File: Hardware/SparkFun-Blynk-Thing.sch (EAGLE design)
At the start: 103 parts, among them IC1 LMV358, Q1 2.5A/30V, Q2 MMBT2222A, Q3 MMBT2222A, U1 MCP73831, U2 ESP8266, U3 AP2112K-3.3V, U4 FT231XS-U, U5 W25Q32FVSS, U6 SI7021, Y1 26MHz

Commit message: Adding PROD_ID's to U5 and JP14
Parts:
- JP14: PROD_ID TBD -> CONN-13230
- U5: PROD_ID (none) -> IC-13229
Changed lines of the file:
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@@
 <grid distance="0.1" unitdist="inch" unit="inch" style="lines" multiple="1" display="no" altdistance="0.01" altunitdist="inch" altunit="inch"/>
 <layers>
-<layer number="1" name="Top" color="4" fill="1" visible="yes" active="no"/>
-<layer number="2" name="Route2" color="1" fill="3" visible="yes" active="no"/>
-<layer number="3" name="Route3" color="4" fill="3" visible="yes" active="no"/>
-<layer number="4" name="Route4" color="1" fill="4" visible="yes" active="no"/>
-<layer number="5" name="Route5" color="4" fill="4" visible="yes" active="no"/>
-<layer number="6" name="Route6" color="1" fill="8" visible="yes" active="no"/>
-<layer number="7" name="Route7" color="4" fill="8" visible="yes" active="no"/>
-<layer number="8" name="Route8" color="1" fill="2" visible="yes" active="no"/>
-<layer number="9" name="Route9" color="4" fill="2" visible="yes" active="no"/>
-<layer number="10" name="Route10" color="1" fill="7" visible="yes" active="no"/>
-<layer number="11" name="Route11" color="4" fill="7" visible="yes" active="no"/>
-<layer number="12" name="Route12" color="1" fill="5" visible="yes" active="no"/>
-<layer number="13" name="Route13" color="4" fill="5" visible="yes" active="no"/>
-<layer number="14" name="Route14" color="1" fill="6" visible="yes" active="no"/>
-<layer number="15" name="Route15" color="4" fill="6" visible="yes" active="no"/>
-<layer number="16" name="Bottom" color="1" fill="1" visible="yes" active="no"/>
-<layer number="17" name="Pads" color="2" fill="1" visible="yes" active="no"/>
-<layer number="18" name="Vias" color="2" fill="1" visible="yes" active="no"/>
-<layer number="19" name="Unrouted" color="6" fill="1" visible="yes" active="no"/>
-<layer number="20" name="Dimension" color="15" fill="1" visible="yes" active="no"/>
-<layer number="21" name="tPlace" color="16" fill="1" visible="yes" active="no"/>
-<layer number="22" name="bPlace" color="14" fill="1" visible="yes" active="no"/>
-<layer number="23" name="tOrigins" color="15" fill="1" visible="yes" active="no"/>
-<layer number="24" name="bOrigins" color="15" fill="1" visible="yes" active="no"/>
-<layer number="25" name="tNames" color="7" fill="1" visible="yes" active="no"/>
-<layer number="26" name="bNames" color="7" fill="1" visible="yes" active="no"/>
-<layer number="27" name="tValues" color="7" fill="1" visible="yes" active="no"/>
-<layer number="28" name="bValues" color="7" fill="1" visible="yes" active="no"/>
+<layer number="1" name="Top" color="4" fill="1" visible="no" active="no"/>
+<layer number="2" name="Route2" color="1" fill="3" visible="no" active="no"/>
+<layer number="3" name="Route3" color="4" fill="3" visible="no" active="no"/>
+<layer number="4" name="Route4" color="1" fill="4" visible="no" active="no"/>
+<layer number="5" name="Route5" color="4" fill="4" visible="no" active="no"/>
+<layer number="6" name="Route6" color="1" fill="8" visible="no" active="no"/>
+<layer number="7" name="Route7" color="4" fill="8" visible="no" active="no"/>
+<layer number="8" name="Route8" color="1" fill="2" visible="no" active="no"/>
+<layer number="9" name="Route9" color="4" fill="2" visible="no" active="no"/>
+<layer number="10" name="Route10" color="1" fill="7" visible="no" active="no"/>
+<layer number="11" name="Route11" color="4" fill="7" visible="no" active="no"/>
+<layer number="12" name="Route12" color="1" fill="5" visible="no" active="no"/>
+<layer number="13" name="Route13" color="4" fill="5" visible="no" active="no"/>
+<layer number="14" name="Route14" color="1" fill="6" visible="no" active="no"/>
+<layer number="15" name="Route15" color="4" fill="6" visible="no" active="no"/>
+<layer number="16" name="Bottom" color="1" fill="1" visible="no" active="no"/>
+<layer number="17" name="Pads" color="2" fill="1" visible="no" active="no"/>
+<layer number="18" name="Vias" color="2" fill="1" visible="no" active="no"/>
+<layer number="19" name="Unrouted" color="6" fill="1" visible="no" active="no"/>
+<layer number="20" name="Dimension" color="15" fill="1" visible="no" active="no"/>
+<layer number="21" name="tPlace" color="16" fill="1" visible="no" active="no"/>
+<layer number="22" name="bPlace" color="14" fill="1" visible="no" active="no"/>
+<layer number="23" name="tOrigins" color="15" fill="1" visible="no" active="no"/>
+<layer number="24" name="bOrigins" color="15" fill="1" visible="no" active="no"/>
+<layer number="25" name="tNames" color="7" fill="1" visible="no" active="no"/>
+<layer number="26" name="bNames" color="7" fill="1" visible="no" active="no"/>
+<layer number="27" name="tValues" color="7" fill="1" visible="no" active="no"/>
+<layer number="28" name="bValues" color="7" fill="1" visible="no" active="no"/>
 <layer number="29" name="tStop" color="7" fill="3" visible="no" active="no"/>
 <layer number="30" name="bStop" color="7" fill="6" visible="no" active="no"/>
@@
 <layer number="35" name="tGlue" color="7" fill="4" visible="no" active="no"/>
 <layer number="36" name="bGlue" color="7" fill="5" visible="no" active="no"/>
-<layer number="37" name="tTest" color="7" fill="1" visible="yes" active="no"/>
-<layer number="38" name="bTest" color="7" fill="1" visible="yes" active="no"/>
+<layer number="37" name="tTest" color="7" fill="1" visible="no" active="no"/>
+<layer number="38" name="bTest" color="7" fill="1" visible="no" active="no"/>
 <layer number="39" name="tKeepout" color="4" fill="11" visible="no" active="no"/>
 <layer number="40" name="bKeepout" color="1" fill="11" visible="no" active="no"/>
@@
 <layer number="44" name="Drills" color="7" fill="1" visible="no" active="no"/>
 <layer number="45" name="Holes" color="7" fill="1" visible="no" active="no"/>
-<layer number="46" name="Milling" color="3" fill="1" visible="yes" active="no"/>
-<layer number="47" name="Measures" color="7" fill="1" visible="yes" active="no"/>
-<layer number="48" name="Document" color="7" fill="1" visible="yes" active="no"/>
-<layer number="49" name="Reference" color="7" fill="1" visible="yes" active="no"/>
-<layer number="50" name="dxf" color="7" fill="1" visible="yes" active="no"/>
-<layer number="51" name="tDocu" color="6" fill="1" visible="yes" active="no"/>
-<layer number="52" name="bDocu" color="7" fill="1" visible="yes" active="no"/>
-<layer number="53" name="tGND_GNDA" color="7" fill="9" visible="yes" active="no"/>
-<layer number="54" name="bGND_GNDA" color="1" fill="9" visible="yes" active="no"/>
-<layer number="56" name="wert" color="7" fill="1" visible="yes" active="no"/>
-<layer number="57" name="tCAD" color="7" fill="1" visible="yes" active="no"/>
-<layer number="59" name="tCarbon" color="7" fill="1" visible="yes" active="no"/>
-<layer number="60" name="bCarbon" color="7" fill="1" visible="yes" active="no"/>
+<layer number="46" name="Milling" color="3" fill="1" visible="no" active="no"/>
+<layer number="47" name="Measures" color="7" fill="1" visible="no" active="no"/>
+<layer number="48" name="Document" color="7" fill="1" visible="no" active="no"/>
+<layer number="49" name="Reference" color="7" fill="1" visible="no" active="no"/>
+<layer number="50" name="dxf" color="7" fill="1" visible="no" active="no"/>
+<layer number="51" name="tDocu" color="6" fill="1" visible="no" active="no"/>
+<layer number="52" name="bDocu" color="7" fill="1" visible="no" active="no"/>
+<layer number="53" name="tGND_GNDA" color="7" fill="9" visible="no" active="no"/>
+<layer number="54" name="bGND_GNDA" color="1" fill="9" visible="no" active="no"/>
+<layer number="56" name="wert" color="7" fill="1" visible="no" active="no"/>
+<layer number="57" name="tCAD" color="7" fill="1" visible="no" active="no"/>
+<layer number="59" name="tCarbon" color="7" fill="1" visible="no" active="no"/>
+<layer number="60" name="bCarbon" color="7" fill="1" visible="no" active="no"/>
 <layer number="90" name="Modules" color="5" fill="1" visible="yes" active="yes"/>
 <layer number="91" name="Nets" color="2" fill="1" visible="yes" active="yes"/>
@@
 <part name="SUPPLY15" library="SparkFun-Aesthetics" deviceset="VCC" device=""/>
 <part name="GND36" library="SparkFun-Aesthetics" deviceset="GND" device=""/>
-<part name="U5" library="blynk-thing-temp" deviceset="W25Q32FV" device="SS"/>
+<part name="U5" library="blynk-thing-temp" deviceset="W25Q32FV" device="SS">
+<attribute name="PROD_ID" value="IC-13229"/>
+</part>
 <part name="LOGO2" library="SparkFun-Aesthetics" deviceset="OSHW-LOGO" device="S" value="OSHW-LOGOS"/>
 <part name="E1" library="SparkFun-RF" deviceset="ANTENNA" device="TRACE" value="ANTENNATRACE"/>
@@
 <part name="D4" library="SparkFun-LED" deviceset="WS2812B" device="" value="WS2812"/>
 <part name="JP14" library="SparkFun-Connectors" deviceset="M03" device="JST-PTH-VERT">
-<attribute name="PROD_ID" value="TBD"/>
+<attribute name="PROD_ID" value="CONN-13230"/>
 </part>
 <part name="U6" library="SparkFun-Sensors" deviceset="SI7021" device=""/>

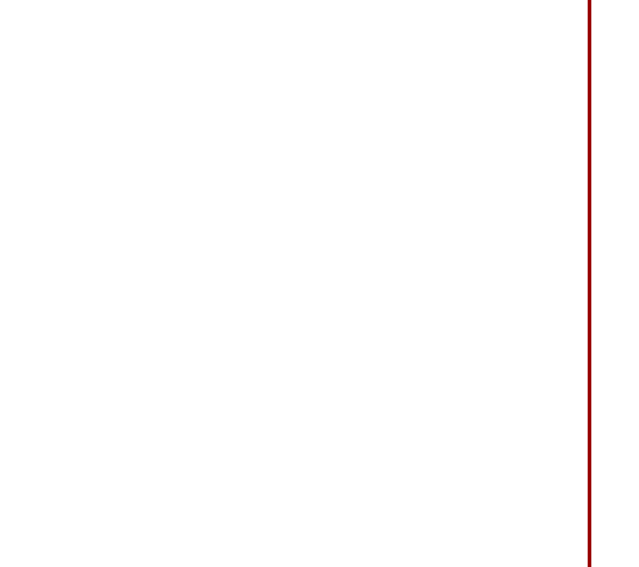
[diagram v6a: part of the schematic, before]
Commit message: Moving WS2812-VCC jumper.
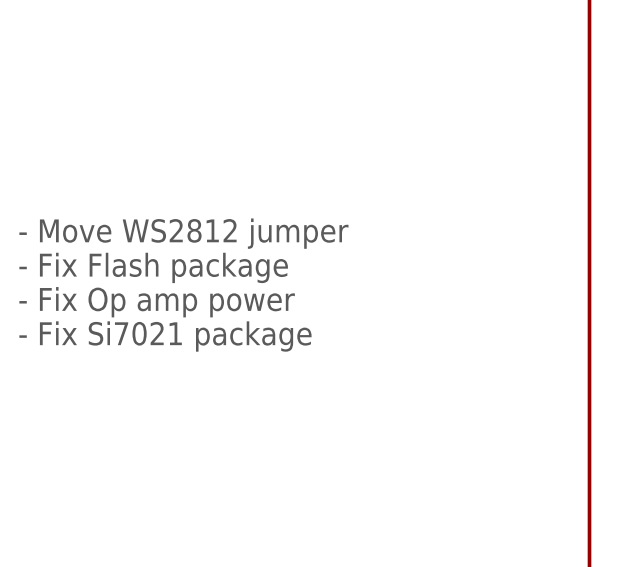
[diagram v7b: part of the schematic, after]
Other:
- note added: "- Move WS2812 jumper - Fix Flash package - Fix Op amp power - Fix Si7021 package"
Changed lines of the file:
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@@
 <grid distance="0.1" unitdist="inch" unit="inch" style="lines" multiple="1" display="no" altdistance="0.01" altunitdist="inch" altunit="inch"/>
 <layers>
-<layer number="1" name="Top" color="4" fill="1" visible="no" active="no"/>
-<layer number="2" name="Route2" color="1" fill="3" visible="no" active="no"/>
-<layer number="3" name="Route3" color="4" fill="3" visible="no" active="no"/>
-<layer number="4" name="Route4" color="1" fill="4" visible="no" active="no"/>
-<layer number="5" name="Route5" color="4" fill="4" visible="no" active="no"/>
-<layer number="6" name="Route6" color="1" fill="8" visible="no" active="no"/>
-<layer number="7" name="Route7" color="4" fill="8" visible="no" active="no"/>
-<layer number="8" name="Route8" color="1" fill="2" visible="no" active="no"/>
-<layer number="9" name="Route9" color="4" fill="2" visible="no" active="no"/>
-<layer number="10" name="Route10" color="1" fill="7" visible="no" active="no"/>
-<layer number="11" name="Route11" color="4" fill="7" visible="no" active="no"/>
-<layer number="12" name="Route12" color="1" fill="5" visible="no" active="no"/>
-<layer number="13" name="Route13" color="4" fill="5" visible="no" active="no"/>
-<layer number="14" name="Route14" color="1" fill="6" visible="no" active="no"/>
-<layer number="15" name="Route15" color="4" fill="6" visible="no" active="no"/>
-<layer number="16" name="Bottom" color="1" fill="1" visible="no" active="no"/>
-<layer number="17" name="Pads" color="2" fill="1" visible="no" active="no"/>
-<layer number="18" name="Vias" color="2" fill="1" visible="no" active="no"/>
-<layer number="19" name="Unrouted" color="6" fill="1" visible="no" active="no"/>
-<layer number="20" name="Dimension" color="15" fill="1" visible="no" active="no"/>
-<layer number="21" name="tPlace" color="16" fill="1" visible="no" active="no"/>
-<layer number="22" name="bPlace" color="14" fill="1" visible="no" active="no"/>
-<layer number="23" name="tOrigins" color="15" fill="1" visible="no" active="no"/>
-<layer number="24" name="bOrigins" color="15" fill="1" visible="no" active="no"/>
-<layer number="25" name="tNames" color="7" fill="1" visible="no" active="no"/>
-<layer number="26" name="bNames" color="7" fill="1" visible="no" active="no"/>
-<layer number="27" name="tValues" color="7" fill="1" visible="no" active="no"/>
-<layer number="28" name="bValues" color="7" fill="1" visible="no" active="no"/>
+<layer number="1" name="Top" color="4" fill="1" visible="yes" active="no"/>
+<layer number="2" name="Route2" color="1" fill="3" visible="yes" active="no"/>
+<layer number="3" name="Route3" color="4" fill="3" visible="yes" active="no"/>
+<layer number="4" name="Route4" color="1" fill="4" visible="yes" active="no"/>
+<layer number="5" name="Route5" color="4" fill="4" visible="yes" active="no"/>
+<layer number="6" name="Route6" color="1" fill="8" visible="yes" active="no"/>
+<layer number="7" name="Route7" color="4" fill="8" visible="yes" active="no"/>
+<layer number="8" name="Route8" color="1" fill="2" visible="yes" active="no"/>
+<layer number="9" name="Route9" color="4" fill="2" visible="yes" active="no"/>
+<layer number="10" name="Route10" color="1" fill="7" visible="yes" active="no"/>
+<layer number="11" name="Route11" color="4" fill="7" visible="yes" active="no"/>
+<layer number="12" name="Route12" color="1" fill="5" visible="yes" active="no"/>
+<layer number="13" name="Route13" color="4" fill="5" visible="yes" active="no"/>
+<layer number="14" name="Route14" color="1" fill="6" visible="yes" active="no"/>
+<layer number="15" name="Route15" color="4" fill="6" visible="yes" active="no"/>
+<layer number="16" name="Bottom" color="1" fill="1" visible="yes" active="no"/>
+<layer number="17" name="Pads" color="2" fill="1" visible="yes" active="no"/>
+<layer number="18" name="Vias" color="2" fill="1" visible="yes" active="no"/>
+<layer number="19" name="Unrouted" color="6" fill="1" visible="yes" active="no"/>
+<layer number="20" name="Dimension" color="15" fill="1" visible="yes" active="no"/>
+<layer number="21" name="tPlace" color="16" fill="1" visible="yes" active="no"/>
+<layer number="22" name="bPlace" color="14" fill="1" visible="yes" active="no"/>
+<layer number="23" name="tOrigins" color="15" fill="1" visible="yes" active="no"/>
+<layer number="24" name="bOrigins" color="15" fill="1" visible="yes" active="no"/>
+<layer number="25" name="tNames" color="7" fill="1" visible="yes" active="no"/>
+<layer number="26" name="bNames" color="7" fill="1" visible="yes" active="no"/>
+<layer number="27" name="tValues" color="7" fill="1" visible="yes" active="no"/>
+<layer number="28" name="bValues" color="7" fill="1" visible="yes" active="no"/>
 <layer number="29" name="tStop" color="7" fill="3" visible="no" active="no"/>
 <layer number="30" name="bStop" color="7" fill="6" visible="no" active="no"/>
@@
 <layer number="35" name="tGlue" color="7" fill="4" visible="no" active="no"/>
 <layer number="36" name="bGlue" color="7" fill="5" visible="no" active="no"/>
-<layer number="37" name="tTest" color="7" fill="1" visible="no" active="no"/>
-<layer number="38" name="bTest" color="7" fill="1" visible="no" active="no"/>
+<layer number="37" name="tTest" color="7" fill="1" visible="yes" active="no"/>
+<layer number="38" name="bTest" color="7" fill="1" visible="yes" active="no"/>
 <layer number="39" name="tKeepout" color="4" fill="11" visible="no" active="no"/>
 <layer number="40" name="bKeepout" color="1" fill="11" visible="no" active="no"/>
@@
 <layer number="44" name="Drills" color="7" fill="1" visible="no" active="no"/>
 <layer number="45" name="Holes" color="7" fill="1" visible="no" active="no"/>
-<layer number="46" name="Milling" color="3" fill="1" visible="no" active="no"/>
-<layer number="47" name="Measures" color="7" fill="1" visible="no" active="no"/>
-<layer number="48" name="Document" color="7" fill="1" visible="no" active="no"/>
-<layer number="49" name="Reference" color="7" fill="1" visible="no" active="no"/>
-<layer number="50" name="dxf" color="7" fill="1" visible="no" active="no"/>
-<layer number="51" name="tDocu" color="6" fill="1" visible="no" active="no"/>
-<layer number="52" name="bDocu" color="7" fill="1" visible="no" active="no"/>
-<layer number="53" name="tGND_GNDA" color="7" fill="9" visible="no" active="no"/>
-<layer number="54" name="bGND_GNDA" color="1" fill="9" visible="no" active="no"/>
-<layer number="56" name="wert" color="7" fill="1" visible="no" active="no"/>
-<layer number="57" name="tCAD" color="7" fill="1" visible="no" active="no"/>
-<layer number="59" name="tCarbon" color="7" fill="1" visible="no" active="no"/>
-<layer number="60" name="bCarbon" color="7" fill="1" visible="no" active="no"/>
+<layer number="46" name="Milling" color="3" fill="1" visible="yes" active="no"/>
+<layer number="47" name="Measures" color="7" fill="1" visible="yes" active="no"/>
+<layer number="48" name="Document" color="7" fill="1" visible="yes" active="no"/>
+<layer number="49" name="Reference" color="7" fill="1" visible="yes" active="no"/>
+<layer number="50" name="dxf" color="7" fill="1" visible="yes" active="no"/>
+<layer number="51" name="tDocu" color="6" fill="1" visible="yes" active="no"/>
+<layer number="52" name="bDocu" color="7" fill="1" visible="yes" active="no"/>
+<layer number="53" name="tGND_GNDA" color="7" fill="9" visible="yes" active="no"/>
+<layer number="54" name="bGND_GNDA" color="1" fill="9" visible="yes" active="no"/>
+<layer number="56" name="wert" color="7" fill="1" visible="yes" active="no"/>
+<layer number="57" name="tCAD" color="7" fill="1" visible="yes" active="no"/>
+<layer number="59" name="tCarbon" color="7" fill="1" visible="yes" active="no"/>
+<layer number="60" name="bCarbon" color="7" fill="1" visible="yes" active="no"/>
 <layer number="90" name="Modules" color="5" fill="1" visible="yes" active="yes"/>
 <layer number="91" name="Nets" color="2" fill="1" visible="yes" active="yes"/>
@@
 <text x="76.2" y="218.44" size="1.524" layer="97">600mA out
 6V max in</text>
+<text x="-63.5" y="53.34" size="2.54" layer="97">- Move WS2812 jumper
+- Fix Flash package
+- Fix Op amp power
+- Fix Si7021 package</text>
 </plain>
 <instances>
